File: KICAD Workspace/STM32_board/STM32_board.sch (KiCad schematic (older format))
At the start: 20 parts, among them J1 Power connector, J2 High side connector, J3 Sensors connector, J4 LCD interface, J5 Low side connector, J6 3v3_out, U1 CD4050BE, U2 LM7805_TO220, U3 LP2950-3.3_TO92

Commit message: Added picture with pin configuration
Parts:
- J1: footprint Connector_PinSocket_2.54mm:PinSocket_1x02_P2.54mm_Vertical -> Connector_Molex:Molex_SPOX_5267-02A_1x02_P2.50mm_Vertical
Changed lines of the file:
@@
 F 0 "J1" H 10273 980 50  0000 R CNN
 F 1 "Power connector" H 10273 1071 50  0000 R CNN
-F 2 "Connector_PinSocket_2.54mm:PinSocket_1x02_P2.54mm_Vertical" H 10300 1100 50  0001 C CNN
+F 2 "Connector_Molex:Molex_SPOX_5267-02A_1x02_P2.50mm_Vertical" H 10300 1100 50  0001 C CNN
 F 3 "~" H 10300 1100 50  0001 C CNN
 	1    10300 1100

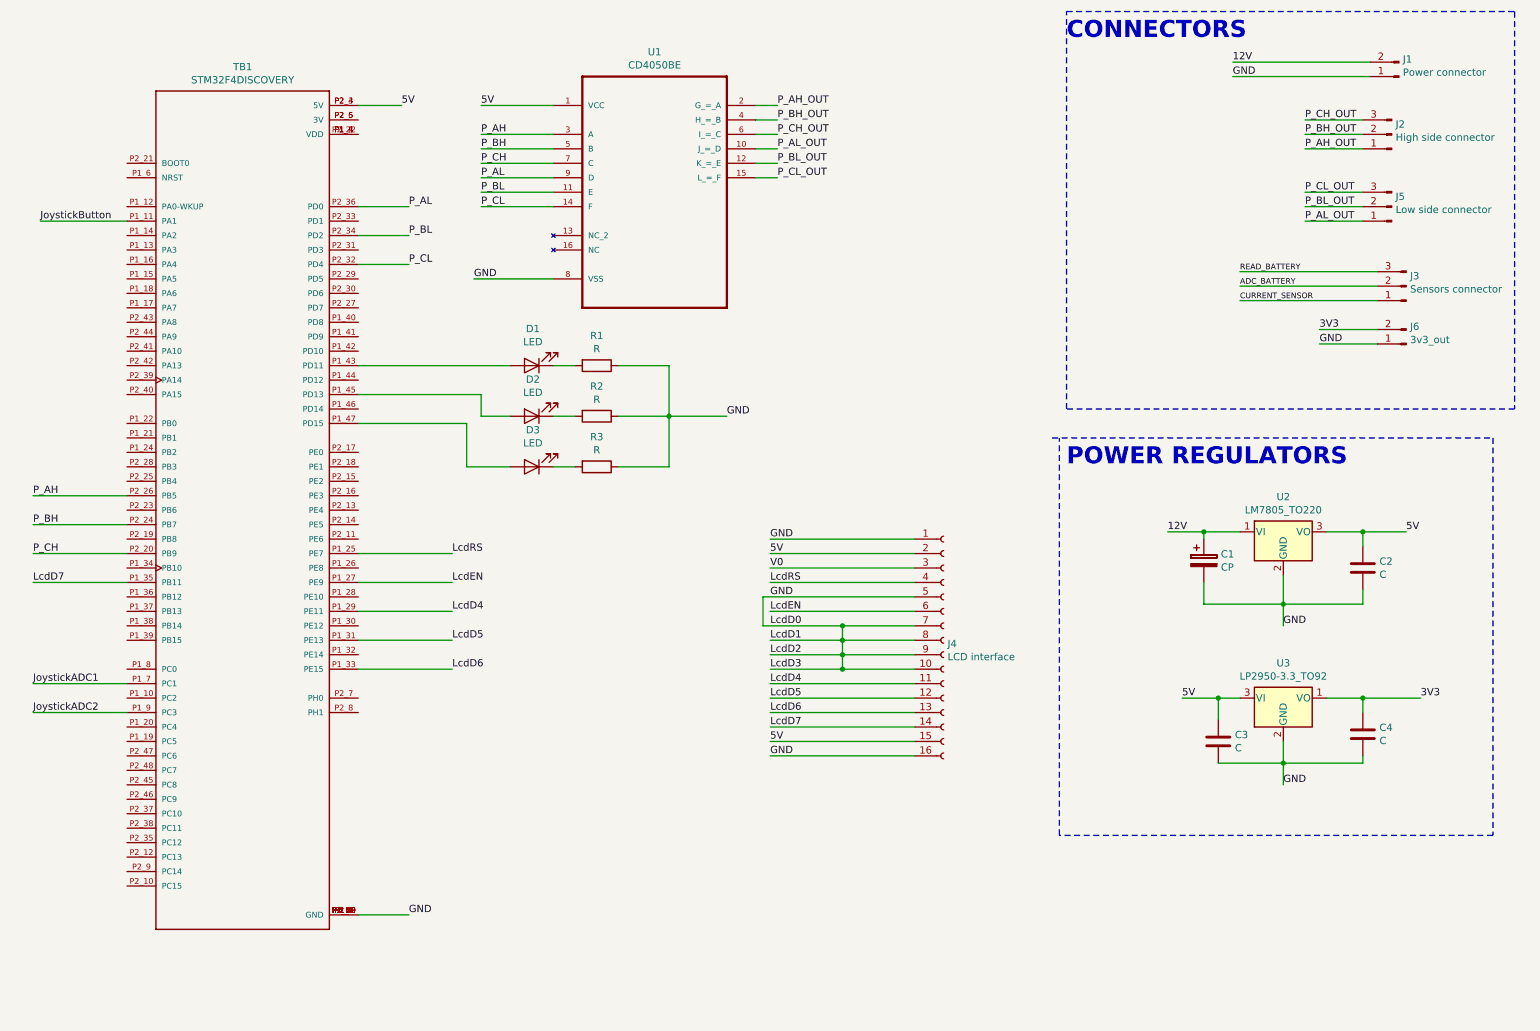
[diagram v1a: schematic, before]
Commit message: Added some footprints and conenctors
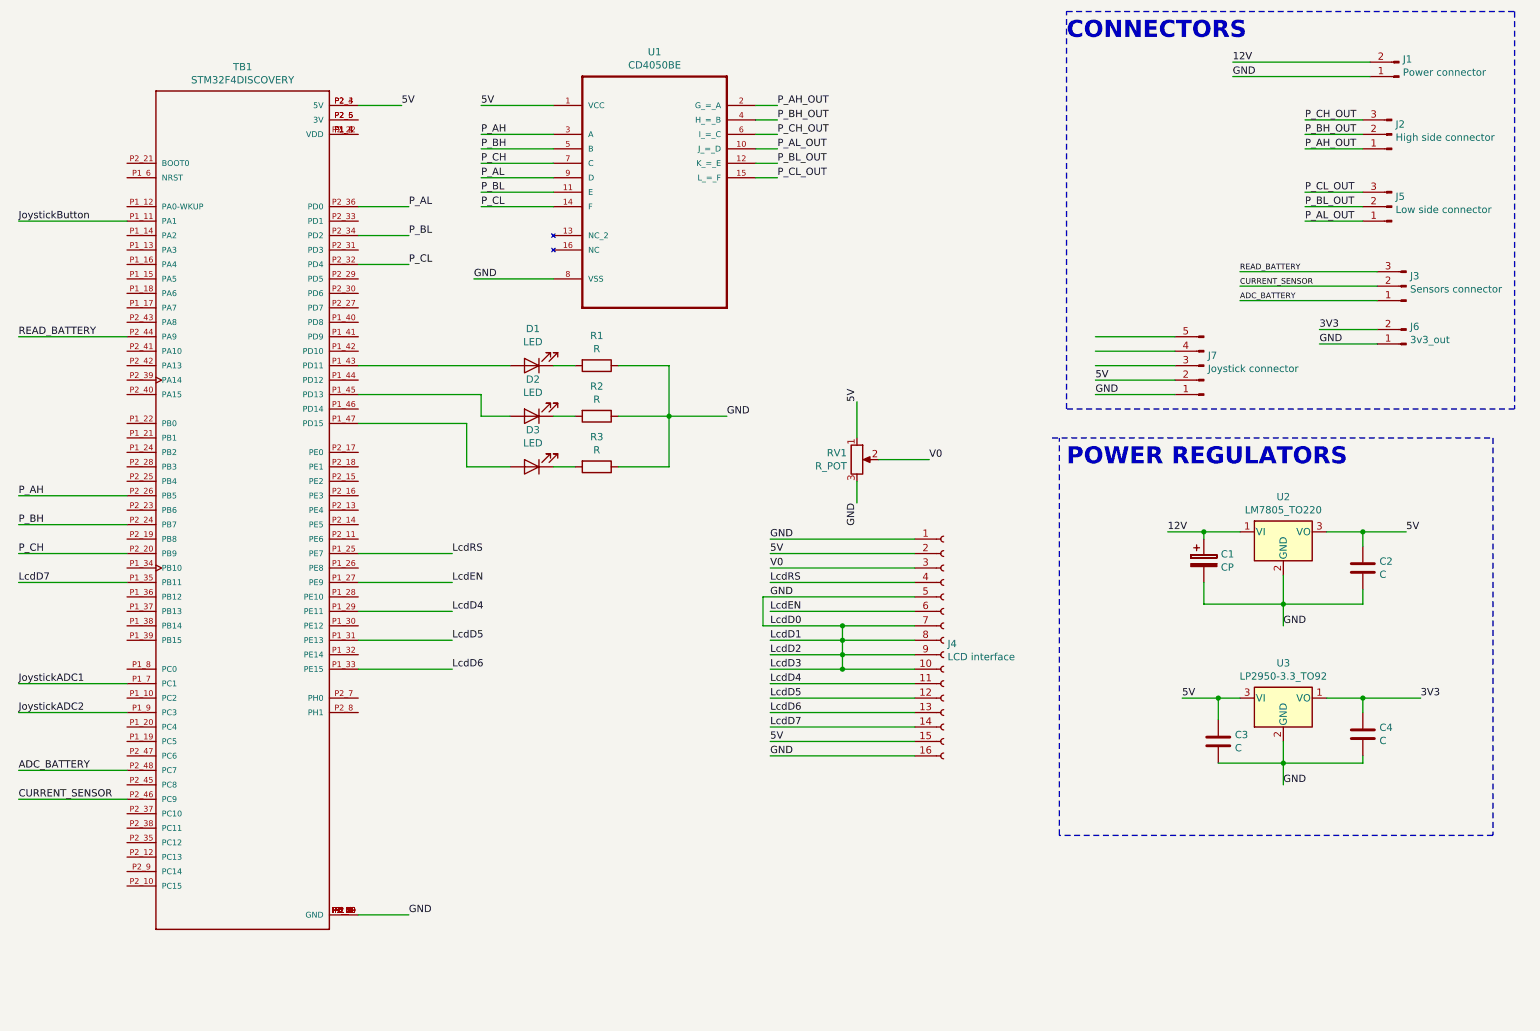
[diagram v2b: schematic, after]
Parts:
- added J7: Joystick connector, Connector_PinSocket_2.54mm:PinSocket_1x05_P2.54mm_Vertical, symbol Connector:Conn_01x05_Male
- added RV1: R_POT, Potentiometer_THT:Potentiometer_Vishay_248GJ-249GJ_Single_Horizontal, symbol Device:R_POT
- C1: footprint (none) -> Capacitor_THT:C_Radial_D4.0mm_H7.0mm_P1.50mm
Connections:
- net 5V: now also J7.2 (Pin_2), RV1.1
- net ADC_BATTERY: now also J3.1 (Pin_1), TB1.P2_48 (PC7); no longer J3.2 (Pin_2)
- net CURRENT_SENSOR: now also J3.2 (Pin_2), TB1.P2_46 (PC9); no longer J3.1 (Pin_1)
- net GND: now also J7.1 (Pin_1), RV1.3
- net READ_BATTERY: now also TB1.P2_44 (PA9)
- net V0: now also RV1.2
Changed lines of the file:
@@
 F 0 "C1" H 9068 4496 50  0000 L CNN
 F 1 "CP" H 9068 4405 50  0000 L CNN
-F 2 "" H 8988 4300 50  0001 C CNN
+F 2 "Capacitor_THT:C_Radial_D4.0mm_H7.0mm_P1.50mm" H 8988 4300 50  0001 C CNN
 F 3 "~" H 8950 4450 50  0001 C CNN
 	1    8950 4450
@@
 Text Label 9200 2450 0    39   ~ 0
 READ_BATTERY
+Text Label 9200 2650 0    39   ~ 0
+ADC_BATTERY
 Text Label 9200 2550 0    39   ~ 0
-ADC_BATTERY
-Text Label 9200 2650 0    39   ~ 0
 CURRENT_SENSOR
-Wire Wire Line
-	1500 5300 850  5300
-Text Label 850  5300 0    50   ~ 0
+Text Label 750  5300 0    50   ~ 0
 JoystickADC1
-Wire Wire Line
-	1500 5500 850  5500
-Text Label 850  5500 0    50   ~ 0
+Text Label 750  5500 0    50   ~ 0
 JoystickADC2
-Wire Wire Line
-	1500 2100 900  2100
-Text Label 900  2100 0    50   ~ 0
+Text Label 750  2100 0    50   ~ 0
 JoystickButton
 Wire Wire Line
@@
 Wire Wire Line
 	3100 5200 3750 5200
-Wire Wire Line
-	1500 4600 850  4600
-Text Label 850  4600 0    50   ~ 0
+Text Label 750  4600 0    50   ~ 0
 LcdD7
 Text Label 3750 4400 0    50   ~ 0
@@
 Text Label 3450 2400 0    50   ~ 0
 P_CL
-Wire Wire Line
-	1500 4000 850  4000
-Wire Wire Line
-	1500 4200 850  4200
-Wire Wire Line
-	1500 4400 850  4400
-Text Label 850  4000 0    50   ~ 0
+Text Label 750  4000 0    50   ~ 0
 P_AH
-Text Label 850  4200 0    50   ~ 0
+Text Label 750  4200 0    50   ~ 0
 P_BH
-Text Label 850  4400 0    50   ~ 0
+Text Label 750  4400 0    50   ~ 0
 P_CH
 $Comp
@@
 Text Label 9750 2950 0    50   ~ 0
 GND
+Text Label 750  2900 0    50   ~ 0
+READ_BATTERY
+Text Label 750  5900 0    50   ~ 0
+ADC_BATTERY
+Text Label 750  6100 0    50   ~ 0
+CURRENT_SENSOR
+Wire Wire Line
+	750  6100 1500 6100
+Wire Wire Line
+	750  5900 1500 5900
+Wire Wire Line
+	750  5300 1500 5300
+Wire Wire Line
+	750  5500 1500 5500
+Wire Wire Line
+	750  4000 1500 4000
+Wire Wire Line
+	750  4200 1500 4200
+Wire Wire Line
+	750  4400 1500 4400
+Wire Wire Line
+	750  4600 1500 4600
+Wire Wire Line
+	750  2900 1500 2900
+Wire Wire Line
+	1500 2100 750  2100
+$Comp
+L Device:R_POT RV1
+U 1 1 5C8864A7
+P 6550 3750
+F 0 "RV1" H 6480 3796 50  0000 R CNN
+F 1 "R_POT" H 6480 3705 50  0000 R CNN
+F 2 "Potentiometer_THT:Potentiometer_Vishay_248GJ-249GJ_Single_Horizontal" H 6550 3750 50  0001 C CNN
+F 3 "~" H 6550 3750 50  0001 C CNN
+	1    6550 3750
+	1    0    0    -1
+$EndComp
+Wire Wire Line
+	6550 3600 6550 3350
+Wire Wire Line
+	6550 3900 6550 4050
+Text Label 6550 3350 1    50   ~ 0
+5V
+Text Label 6550 4050 3    50   ~ 0
+GND
+Wire Wire Line
+	6700 3750 7050 3750
+Text Label 7050 3750 0    50   ~ 0
+V0
+$Comp
+L Connector:Conn_01x05_Male J7
+U 1 1 5C8C99AF
+P 8950 3100
+F 0 "J7" H 8922 3030 50  0000 R CNN
+F 1 "Joystick connector" H 8922 3121 50  0000 R CNN
+F 2 "Connector_PinSocket_2.54mm:PinSocket_1x05_P2.54mm_Vertical" H 8950 3100 50  0001 C CNN
+F 3 "~" H 8950 3100 50  0001 C CNN
+	1    8950 3100
+	-1   0    0    1
+$EndComp
+Wire Wire Line
+	8750 3300 8200 3300
+Text Label 8200 3300 0    50   ~ 0
+GND
+Wire Wire Line
+	8750 3200 8200 3200
+Text Label 8200 3200 0    50   ~ 0
+5V
+Wire Wire Line
+	8750 3100 8200 3100
+Wire Wire Line
+	8750 3000 8200 3000
+Wire Wire Line
+	8750 2900 8200 2900
 $EndSCHEMATC

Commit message: Added some footprints.
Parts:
- C2: footprint (none) -> Capacitor_THT:CP_Radial_D5.0mm_P2.50mm
- C3: value C -> C3; footprint (none) -> Capacitor_THT:CP_Radial_D5.0mm_P2.50mm
- C4: value C -> C4; footprint (none) -> Capacitor_THT:CP_Radial_D5.0mm_P2.50mm
- RV1: footprint Potentiometer_THT:Potentiometer_Vishay_248GJ-249GJ_Single_Horizontal -> Potentiometer_THT:Potentiometer_Alps_RK163_Single_Horizontal
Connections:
- net JoystickADC1: now also J7.3 (Pin_3), TB1.P1_8 (PC0); no longer TB1.P1_7 (PC1)
- net JoystickADC2: now also J7.4 (Pin_4), TB1.P1_10 (PC2); no longer TB1.P1_9 (PC3)
- net JoystickButton: now also J7.5 (Pin_5), TB1.P1_14 (PA2); no longer TB1.P1_11 (PA1)
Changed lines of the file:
@@
 F 0 "C2" H 10165 4546 50  0000 L CNN
 F 1 "C" H 10165 4455 50  0000 L CNN
-F 2 "" H 10088 4350 50  0001 C CNN
+F 2 "Capacitor_THT:CP_Radial_D5.0mm_P2.50mm" H 10088 4350 50  0001 C CNN
 F 3 "~" H 10050 4500 50  0001 C CNN
 	1    10050 4500
@@
 	1    0    0    -1
 $EndComp
-Wire Wire Line
-	9200 5400 9050 5400
 Text Label 8800 5400 0    50   ~ 0
 5V
@@
 Text Label 9500 6000 0    50   ~ 0
 GND
-$Comp
-L Device:C C3
-U 1 1 5C7C47F5
-P 9050 5700
-F 0 "C3" H 9165 5746 50  0000 L CNN
-F 1 "C" H 9165 5655 50  0000 L CNN
-F 2 "" H 9088 5550 50  0001 C CNN
-F 3 "~" H 9050 5700 50  0001 C CNN
-	1    9050 5700
-	1    0    0    -1
-$EndComp
-Wire Wire Line
-	9050 5550 9050 5400
-Connection ~ 9050 5400
-Wire Wire Line
-	9050 5400 8800 5400
 Wire Wire Line
 	9050 5850 9500 5850
@@
 P 10050 5650
 F 0 "C4" H 10165 5696 50  0000 L CNN
-F 1 "C" H 10165 5605 50  0000 L CNN
-F 2 "" H 10088 5500 50  0001 C CNN
+F 1 "C4" H 10165 5605 50  0000 L CNN
+F 2 "Capacitor_THT:CP_Radial_D5.0mm_P2.50mm" H 10088 5500 50  0001 C CNN
 F 3 "~" H 10050 5650 50  0001 C CNN
 	1    10050 5650
@@
 Text Label 9200 2550 0    39   ~ 0
 CURRENT_SENSOR
-Text Label 750  5300 0    50   ~ 0
+Text Label 750  5200 0    50   ~ 0
 JoystickADC1
-Text Label 750  5500 0    50   ~ 0
+Text Label 750  5400 0    50   ~ 0
 JoystickADC2
-Text Label 750  2100 0    50   ~ 0
+Text Label 750  2200 0    50   ~ 0
 JoystickButton
 Wire Wire Line
@@
 	750  5900 1500 5900
 Wire Wire Line
-	750  5300 1500 5300
-Wire Wire Line
-	750  5500 1500 5500
-Wire Wire Line
 	750  4000 1500 4000
 Wire Wire Line
@@
 Wire Wire Line
 	750  2900 1500 2900
-Wire Wire Line
-	1500 2100 750  2100
 $Comp
 L Device:R_POT RV1
@@
 F 0 "RV1" H 6480 3796 50  0000 R CNN
 F 1 "R_POT" H 6480 3705 50  0000 R CNN
-F 2 "Potentiometer_THT:Potentiometer_Vishay_248GJ-249GJ_Single_Horizontal" H 6550 3750 50  0001 C CNN
+F 2 "Potentiometer_THT:Potentiometer_Alps_RK163_Single_Horizontal" H 6550 3750 50  0001 C CNN
 F 3 "~" H 6550 3750 50  0001 C CNN
 	1    6550 3750
@@
 Wire Wire Line
 	8750 2900 8200 2900
+Wire Wire Line
+	750  2200 1500 2200
+Wire Wire Line
+	750  5400 1500 5400
+Wire Wire Line
+	1500 5200 750  5200
+Text Label 8200 2900 0    50   ~ 0
+JoystickButton
+Text Label 8200 3100 0    50   ~ 0
+JoystickADC1
+Text Label 8200 3000 0    50   ~ 0
+JoystickADC2
+Wire Wire Line
+	9050 5400 8800 5400
+Wire Wire Line
+	9200 5400 9050 5400
+Connection ~ 9050 5400
+Wire Wire Line
+	9050 5550 9050 5400
+$Comp
+L Device:C C3
+U 1 1 5C7C47F5
+P 9050 5700
+F 0 "C3" H 9165 5746 50  0000 L CNN
+F 1 "C3" H 9165 5655 50  0000 L CNN
+F 2 "Capacitor_THT:CP_Radial_D5.0mm_P2.50mm" H 9088 5550 50  0001 C CNN
+F 3 "~" H 9050 5700 50  0001 C CNN
+	1    9050 5700
+	1    0    0    -1
+$EndComp
 $EndSCHEMATC

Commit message: Added modified PCB
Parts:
- added J8: External Pins, Connector_PinHeader_2.54mm:PinHeader_1x07_P2.54mm_Vertical, symbol Connector:Conn_01x07_Female
- added J9: UART module, Connector_PinHeader_2.54mm:PinHeader_1x06_P2.54mm_Vertical, symbol Connector:Conn_01x06_Female
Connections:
- net GND: now also J9.6 (Pin_6)
- net EXT_1: now reaches TB1.P1_18 (PA6)
- net EXT_1: now also J8.1 (Pin_1)
- net EXT_2: now reaches TB1.P1_20 (PC4)
- net EXT_2: now also J8.2 (Pin_2)
- net EXT_3: now reaches TB1.P1_22 (PB0)
- net EXT_3: now also J8.3 (Pin_3)
- net EXT_4: now reaches TB1.P1_24 (PB2)
- net EXT_4: now also J8.4 (Pin_4)
- net EXT_5: now reaches TB1.P1_26 (PE8)
- net EXT_5: now also J8.5 (Pin_5)
- net EXT_6: now reaches TB1.P1_28 (PE10)
- net EXT_6: now also J8.6 (Pin_6)
- net EXT_7: now reaches TB1.P1_30 (PE12)
- net EXT_7: now also J8.7 (Pin_7)
- net UART1_TX: now reaches TB1.P2_37 (PC10)
- net UART1_TX: now also J9.3 (Pin_3)
- net UART2_RX: now reaches TB1.P2_38 (PC11)
- net UART2_RX: now also J9.2 (Pin_2)
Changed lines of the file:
@@
 	1    0    0    -1
 $EndComp
+$Comp
+L Connector:Conn_01x07_Female J8
+U 1 1 5C87FF0E
+P 6000 6500
+F 0 "J8" H 6027 6526 50  0000 L CNN
+F 1 "External Pins" H 6027 6435 50  0000 L CNN
+F 2 "Connector_PinHeader_2.54mm:PinHeader_1x07_P2.54mm_Vertical" H 6000 6500 50  0001 C CNN
+F 3 "~" H 6000 6500 50  0001 C CNN
+	1    6000 6500
+	1    0    0    -1
+$EndComp
+Wire Wire Line
+	5800 6200 5050 6200
+Wire Wire Line
+	5800 6300 5050 6300
+Wire Wire Line
+	5800 6400 5050 6400
+Wire Wire Line
+	5800 6500 5050 6500
+Wire Wire Line
+	5800 6600 5050 6600
+Wire Wire Line
+	5800 6700 5050 6700
+Wire Wire Line
+	5800 6800 5050 6800
+Wire Wire Line
+	1500 2600 700  2600
+Text Label 700  2600 0    50   ~ 0
+EXT_1
+Text Label 5050 6200 0    50   ~ 0
+EXT_1
+Wire Wire Line
+	1500 5600 750  5600
+Text Label 750  5600 0    50   ~ 0
+EXT_2
+Text Label 5050 6300 0    50   ~ 0
+EXT_2
+Text Label 5050 6400 0    50   ~ 0
+EXT_3
+Text Label 5050 6500 0    50   ~ 0
+EXT_4
+Text Label 5050 6600 0    50   ~ 0
+EXT_5
+Text Label 5050 6700 0    50   ~ 0
+EXT_6
+Text Label 5050 6800 0    50   ~ 0
+EXT_7
+Wire Wire Line
+	1500 3500 750  3500
+Text Label 750  3500 0    50   ~ 0
+EXT_3
+Wire Wire Line
+	1500 3700 750  3700
+Text Label 750  3700 0    50   ~ 0
+EXT_4
+Wire Wire Line
+	3100 4500 3750 4500
+Text Label 3750 4500 0    50   ~ 0
+EXT_5
+Wire Wire Line
+	3100 4700 3750 4700
+Text Label 3750 4700 0    50   ~ 0
+EXT_6
+Wire Wire Line
+	3100 4900 3750 4900
+Text Label 3750 4900 0    50   ~ 0
+EXT_7
+$Comp
+L Connector:Conn_01x06_Female J9
+U 1 1 5C8E1B7B
+P 5850 7300
+F 0 "J9" H 5878 7276 50  0000 L CNN
+F 1 "UART module" H 5878 7185 50  0000 L CNN
+F 2 "Connector_PinHeader_2.54mm:PinHeader_1x06_P2.54mm_Vertical" H 5850 7300 50  0001 C CNN
+F 3 "~" H 5850 7300 50  0001 C CNN
+	1    5850 7300
+	1    0    0    -1
+$EndComp
+Wire Wire Line
+	1500 6200 750  6200
+Wire Wire Line
+	1500 6300 750  6300
+Text Label 750  6200 0    50   ~ 0
+UART1_TX
+Text Label 750  6300 0    50   ~ 0
+UART2_RX
+Wire Wire Line
+	5650 7100 5100 7100
+Wire Wire Line
+	5650 7200 5100 7200
+Wire Wire Line
+	5650 7300 5100 7300
+Wire Wire Line
+	5650 7400 5100 7400
+Wire Wire Line
+	5650 7500 5100 7500
+Text Label 5100 7300 0    50   ~ 0
+UART1_TX
+Text Label 5100 7200 0    50   ~ 0
+UART2_RX
+Text Label 5100 7600 0    50   ~ 0
+GND
+Wire Wire Line
+	5650 7600 5100 7600
 $EndSCHEMATC
